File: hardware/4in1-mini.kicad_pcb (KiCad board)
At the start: 6 copper layers, 31.2 x 33 mm, 191 parts, among them J1 SM08B-SRSS-TB, Q1 DOY180N03T, Q10 DOY180N03T, Q11 DOY180N03T, Q12 DOY180N03T, Q13 DOY180N03T, Q14 DOY180N03T, Q15 DOY180N03T, Q16 DOY180N03T, Q17 DOY180N03T, Q18 DOY180N03T, Q19 DOY180N03T, Q2 DOY180N03T, Q20 DOY180N03T, Q21 DOY180N03T, Q22 DOY180N03T, Q23 DOY180N03T, Q24 DOY180N03T, Q3 DOY180N03T, Q4 DOY180N03T, Q5 DOY180N03T, Q6 DOY180N03T, Q7 DOY180N03T, Q8 DOY180N03T, Q9 DOY180N03T, U1 TLV76733DRVR, U10 AT32F421G8U7, U11 NSG2065Q, U12 INA186A3IDCKR, U13 LMR54406DBVR, U2 AT32F421G8U7, U3 NSG2065Q, U5 FTC160808S4R7MBCA, U6 AT32F421G8U7, U7 NSG2065Q, U8 AT32F421G8U7, U9 NSG2065Q

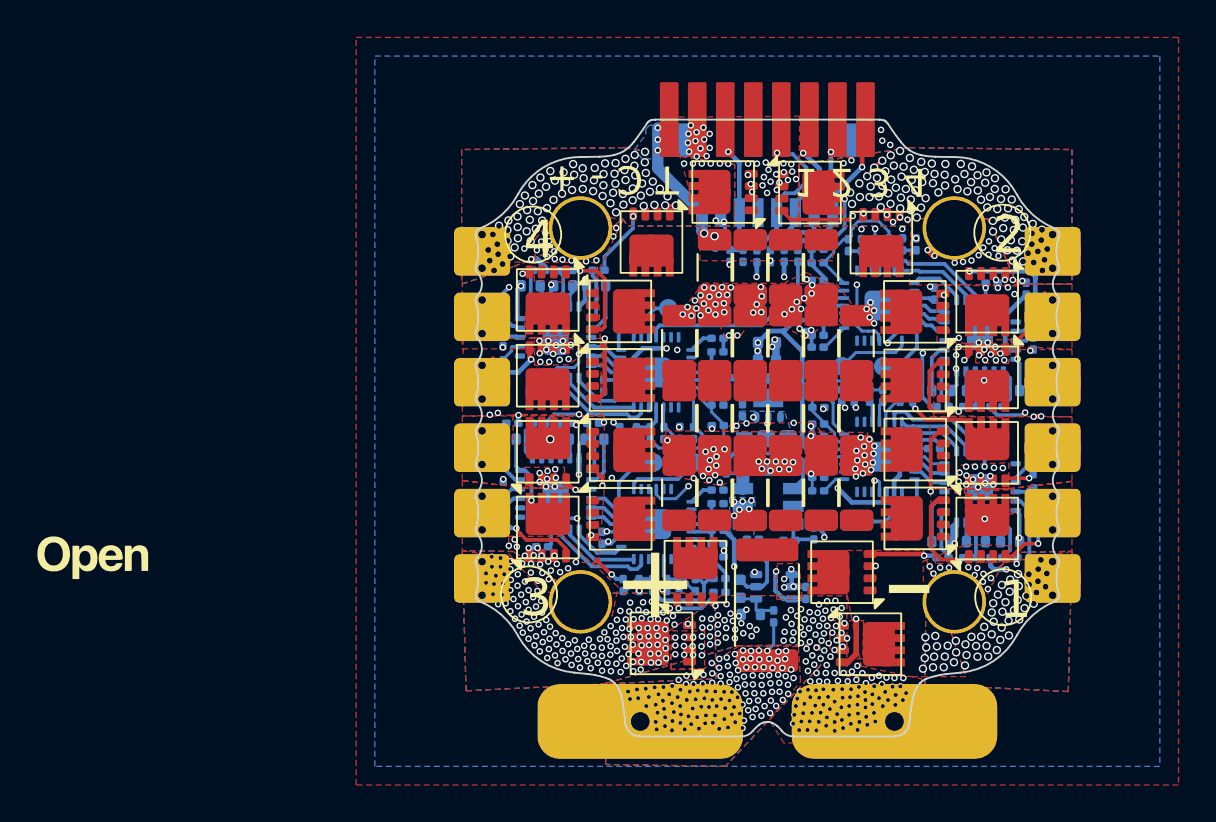
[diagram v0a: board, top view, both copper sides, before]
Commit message: Rebrand silkscreen to incutec, add via stitching, 4.7uF bulk caps
Board state for the batch-1 quote round: OpenDrone silkscreen replaced
with incutec (Stan), added via cluster near the FET bank (Stan), bulk
cap bank fields swapped to FH 1206B475K500NT 4.7uF 50V C29823 (from
the committed schematic change). Fabrication Toolkit archive name
moved to the org standard OpenESC-20x20-rev3.2.

Co-Authored-By: Claude Fable 5 <noreply@anthropic.com>
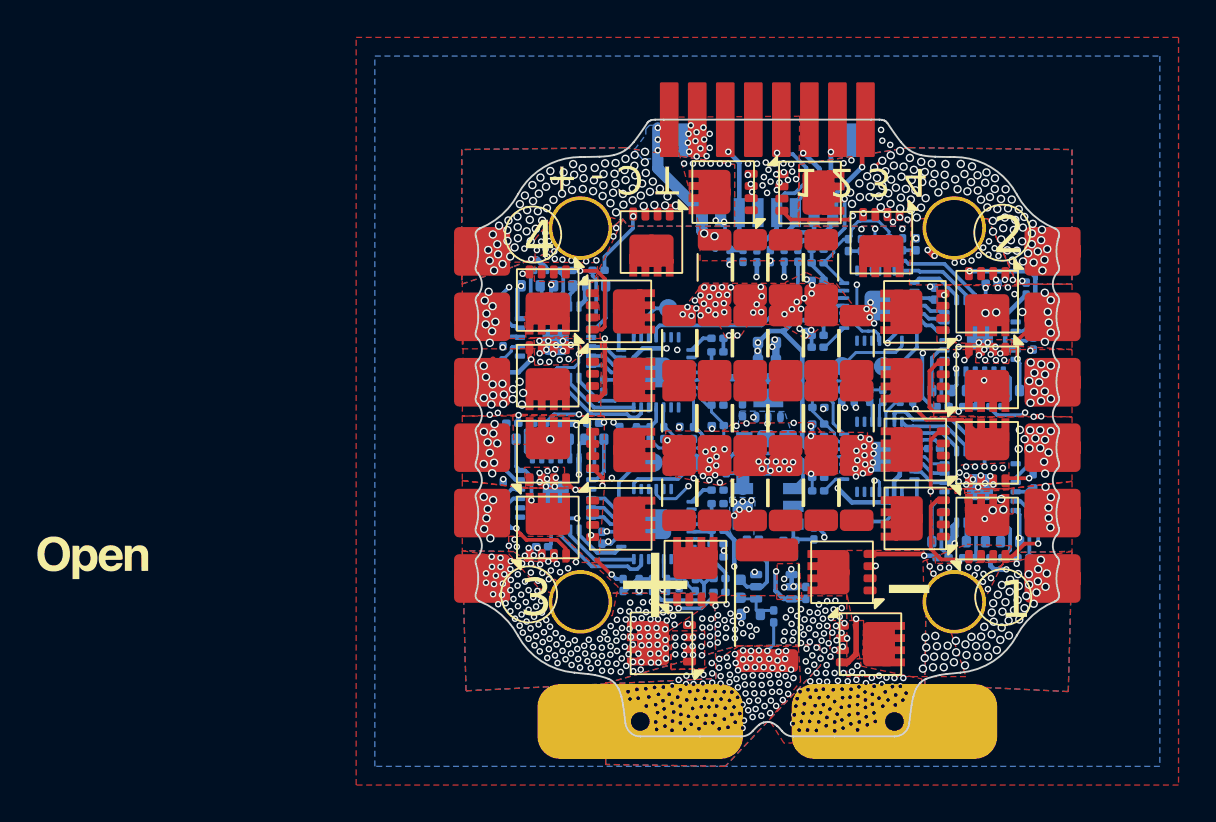
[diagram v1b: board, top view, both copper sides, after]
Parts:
- CL32, CL33, CL34, CL35, CL36, CL38, CL39, CL40, CL42, CL43, CL44, CL45, CL46, CL47, CL48, CL49, CL50 (x2), CL51 (x2), CL54, CL55: value 10uF -> 4.7uF
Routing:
- net /ESC4/MotorC: vias 2 -> 16
- net /ESC4/MotorB: vias 2 -> 10
- net /ESC3/MotorC: vias 2 -> 8
- net /ESC3/MotorB: vias 2 -> 11
- net /ESC2/MotorC: vias 2 -> 11
- net /ESC2/MotorB: vias 2 -> 14
- net /ESC1/MotorC: vias 2 -> 15
- net /ESC1/MotorB: vias 2 -> 10

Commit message: Sync silkscreen rev text to rev3.2 (pipeline rev sync)
Co-Authored-By: Claude Fable 5 <noreply@anthropic.com>
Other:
- board text added: "rev3.2"
- board text removed: "rev3.1"
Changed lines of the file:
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@@
 	)
 	(paper "A4")
+	(title_block
+		(rev "rev3.2")
+	)
 	(layers
 		(0 "F.Cu" signal)
@@
 		)
 	)
-	(gr_text "rev3.1"
+	(gr_text "rev3.2"
 		(at 80.4 38.75 0)
 		(layer "B.SilkS")
@@
 			(justify right bottom mirror)
 		)
-		(render_cache "rev3.1" 0
+		(render_cache "rev3.2" 0
 			(polygon
 				(pts
-					(xy 84.031402 38.495) (xy 83.785663 38.495) (xy 83.785663 37.879508) (xy 83.755804 37.879508) (xy 83.615945 38.495)
-					(xy 83.363794 38.495) (xy 83.51089 37.845619) (xy 83.479382 37.818416) (xy 83.444111 37.774597)
-					(xy 83.423406 37.726226) (xy 83.416368 37.671596) (xy 83.416368 37.30285) (xy 83.662107 37.30285)
-					(xy 83.662107 37.598231) (xy 83.672731 37.623236) (xy 83.696178 37.633586) (xy 83.785663 37.633586)
-					(xy 83.785663 37.269603) (xy 83.696178 37.269603) (xy 83.672731 37.279036) (xy 83.662107 37.30285)
-					(xy 83.416368 37.30285) (xy 83.416368 37.233333) (xy 83.423379 37.177251) (xy 83.443864 37.128238)
-					(xy 83.478466 37.084497) (xy 83.522874 37.05053) (xy 83.571817 37.030499) (xy 83.626936 37.023681)
-					(xy 84.031402 37.023681)
+					(xy 84.39337 38.495) (xy 84.147631 38.495) (xy 84.147631 37.879508) (xy 84.117772 37.879508) (xy 83.977913 38.495)
+					(xy 83.725762 38.495) (xy 83.872858 37.845619) (xy 83.84135 37.818416) (xy 83.806079 37.774597)
+					(xy 83.785374 37.726226) (xy 83.778336 37.671596) (xy 83.778336 37.30285) (xy 84.024075 37.30285)
+					(xy 84.024075 37.598231) (xy 84.034699 37.623236) (xy 84.058146 37.633586) (xy 84.147631 37.633586)
+					(xy 84.147631 37.269603) (xy 84.058146 37.269603) (xy 84.034699 37.279036) (xy 84.024075 37.30285)
+					(xy 83.778336 37.30285) (xy 83.778336 37.233333) (xy 83.785347 37.177251) (xy 83.805832 37.128238)
+					(xy 83.840434 37.084497) (xy 83.884842 37.05053) (xy 83.933785 37.030499) (xy 83.988904 37.023681)
+					(xy 84.39337 37.023681)
 				)
 			)
 			(polygon
 				(pts
-					(xy 82.650941 37.269603) (xy 83.017763 37.269603) (xy 83.017763 37.633586) (xy 82.77404 37.633586)
-					(xy 82.77404 37.879508) (xy 83.017763 37.879508) (xy 83.017763 38.249077) (xy 82.650941 38.249077)
-					(xy 82.650941 38.495) (xy 83.263502 38.495) (xy 83.263502 37.023681) (xy 82.650941 37.023681)
+					(xy 83.012909 37.269603) (xy 83.379731 37.269603) (xy 83.379731 37.633586) (xy 83.136008 37.633586)
+					(xy 83.136008 37.879508) (xy 83.379731 37.879508) (xy 83.379731 38.249077) (xy 83.012909 38.249077)
+					(xy 83.012909 38.495) (xy 83.62547 38.495) (xy 83.62547 37.023681) (xy 83.012909 37.023681)
 				)
 			)
 			(polygon
 				(pts
-					(xy 82.180529 37.023681) (xy 81.934791 37.023681) (xy 81.934791 38.11453) (xy 81.941905 38.191204)
-					(xy 81.962704 38.260666) (xy 81.997189 38.324446) (xy 82.04644 38.383625) (xy 82.105689 38.432735)
-					(xy 82.169568 38.46714) (xy 82.23916 38.487898) (xy 82.315993 38.495) (xy 82.549825 38.495) (xy 82.549825 37.023681)
-					(xy 82.304086 37.023681) (xy 82.304086 38.249077) (xy 82.256681 38.240135) (xy 82.216799 38.213357)
-					(xy 82.189577 38.173902) (xy 82.180529 38.12717)
+					(xy 82.542497 37.023681) (xy 82.296759 37.023681) (xy 82.296759 38.11453) (xy 82.303873 38.191204)
+					(xy 82.324672 38.260666) (xy 82.359157 38.324446) (xy 82.408408 38.383625) (xy 82.467657 38.432735)
+					(xy 82.531536 38.46714) (xy 82.601128 38.487898) (xy 82.677961 38.495) (xy 82.911793 38.495) (xy 82.911793 37.023681)
+					(xy 82.666054 37.023681) (xy 82.666054 38.249077) (xy 82.618649 38.240135) (xy 82.578767 38.213357)
+					(xy 82.551545 38.173902) (xy 82.542497 38.12717)
 				)
 			)
 			(polygon
 				(pts
-					(xy 81.60204 38.495) (xy 81.658501 38.488078) (xy 81.70776 38.467893) (xy 81.751608 38.433908)
-					(xy 81.785588 38.390058) (xy 81.805775 38.34077) (xy 81.8127 38.284248) (xy 81.8127 38.004071)
-					(xy 81.566961 38.004071) (xy 81.566961 38.249077) (xy 81.443405 38.249077) (xy 81.443405 37.978792)
-					(xy 81.450503 37.941421) (xy 81.471981 37.909091) (xy 81.503849 37.886954) (xy 81.542781 37.879508)
-					(xy 81.690884 37.879508) (xy 81.690884 37.633586) (xy 81.542781 37.633586) (xy 81.503805 37.62626)
-					(xy 81.471981 37.604551) (xy 81.450492 37.572679) (xy 81.443405 37.535858) (xy 81.443405 37.269603)
-					(xy 81.566961 37.269603) (xy 81.566961 37.510853) (xy 81.8127 37.510853) (xy 81.8127 37.232783)
-					(xy 81.805785 37.176761) (xy 81.785611 37.127867) (xy 81.751608 37.084314) (xy 81.707793 37.050603)
-					(xy 81.658532 37.030559) (xy 81.60204 37.023681) (xy 81.408325 37.023681) (xy 81.353201 37.03049)
-					(xy 81.304258 37.050494) (xy 81.259856 37.084405) (xy 81.225197 37.128095) (xy 81.204685 37.177046)
-					(xy 81.197666 37.233058) (xy 81.197666 37.547215) (xy 81.204764 37.603171) (xy 81.225526 37.652119)
-					(xy 81.26068 37.695867) (xy 81.321588 37.756592) (xy 81.26068 37.817775) (xy 81.22555 37.861821)
-					(xy 81.204774 37.911162) (xy 81.197666 37.967618) (xy 81.197666 38.283974) (xy 81.204696 38.340485)
-					(xy 81.22522 38.38983) (xy 81.259856 38.433817) (xy 81.30429 38.468003) (xy 81.353231 38.488146)
-					(xy 81.408325 38.495)
+					(xy 81.964008 38.495) (xy 82.020469 38.488078) (xy 82.069728 38.467893) (xy 82.113576 38.433908)
+					(xy 82.147556 38.390058) (xy 82.167743 38.34077) (xy 82.174668 38.284248) (xy 82.174668 38.004071)
+					(xy 81.928929 38.004071) (xy 81.928929 38.249077) (xy 81.805373 38.249077) (xy 81.805373 37.978792)
+					(xy 81.812471 37.941421) (xy 81.833949 37.909091) (xy 81.865817 37.886954) (xy 81.904749 37.879508)
+					(xy 82.052852 37.879508) (xy 82.052852 37.633586) (xy 81.904749 37.633586) (xy 81.865773 37.62626)
+					(xy 81.833949 37.604551) (xy 81.81246 37.572679) (xy 81.805373 37.535858) (xy 81.805373 37.269603)
+					(xy 81.928929 37.269603) (xy 81.928929 37.510853) (xy 82.174668 37.510853) (xy 82.174668 37.232783)
+					(xy 82.167753 37.176761) (xy 82.147579 37.127867) (xy 82.113576 37.084314) (xy 82.069761 37.050603)
+					(xy 82.0205 37.030559) (xy 81.964008 37.023681) (xy 81.770293 37.023681) (xy 81.715169 37.03049)
+					(xy 81.666226 37.050494) (xy 81.621824 37.084405) (xy 81.587165 37.128095) (xy 81.566653 37.177046)
+					(xy 81.559634 37.233058) (xy 81.559634 37.547215) (xy 81.566732 37.603171) (xy 81.587494 37.652119)
+					(xy 81.622648 37.695867) (xy 81.683556 37.756592) (xy 81.622648 37.817775) (xy 81.587518 37.861821)
+					(xy 81.566742 37.911162) (xy 81.559634 37.967618) (xy 81.559634 38.283974) (xy 81.566664 38.340485)
+					(xy 81.587188 38.38983) (xy 81.621824 38.433817) (xy 81.666258 38.468003) (xy 81.715199 38.488146)
+					(xy 81.770293 38.495)
 				)
 			)
 			(polygon
 				(pts
-					(xy 80.837163 38.495) (xy 81.082902 38.495) (xy 81.082902 38.249077) (xy 80.837163 38.249077)
+					(xy 81.199131 38.495) (xy 81.44487 38.495) (xy 81.44487 38.249077) (xy 81.199131 38.249077)
 				)
 			)
 			(polygon
 				(pts
-					(xy 80.470799 38.495) (xy 80.716538 38.495) (xy 80.716538 37.145588) (xy 80.594722 37.023681) (xy 80.470799 37.023681)
+					(xy 81.084368 38.495) (xy 81.084368 37.842596) (xy 81.07749 37.787411) (xy 81.05733 37.738732)
+					(xy 81.023185 37.69486) (xy 80.979265 37.660767) (xy 80.929946 37.640526) (xy 80.873433 37.633586)
+					(xy 80.715072 37.633586) (xy 80.715072 37.269603) (xy 80.838629 37.269603) (xy 80.838629 37.510853)
+					(xy 81.084368 37.510853) (xy 81.084368 37.232783) (xy 81.077462 37.176755) (xy 81.057316 37.12786)
+					(xy 81.023368 37.084314) (xy 80.979552 37.050603) (xy 80.930292 37.030559) (xy 80.8738 37.023681)
+					(xy 80.679993 37.023681) (xy 80.624875 37.030499) (xy 80.575932 37.05053) (xy 80.531524 37.084497)
+					(xy 80.496871 37.128247) (xy 80.476356 37.177288) (xy 80.469334 37.233424) (xy 80.469334 37.671871)
+					(xy 80.476307 37.726607) (xy 80.496793 37.774979) (xy 80.531616 37.818691) (xy 80.576084 37.852651)
+					(xy 80.625117 37.872686) (xy 80.680359 37.879508) (xy 80.838629 37.879508) (xy 80.838629 38.249077)
+					(xy 80.715072 38.249077) (xy 80.715072 38.004071) (xy 80.469334 38.004071) (xy 80.469334 38.495)
 				)
 			)

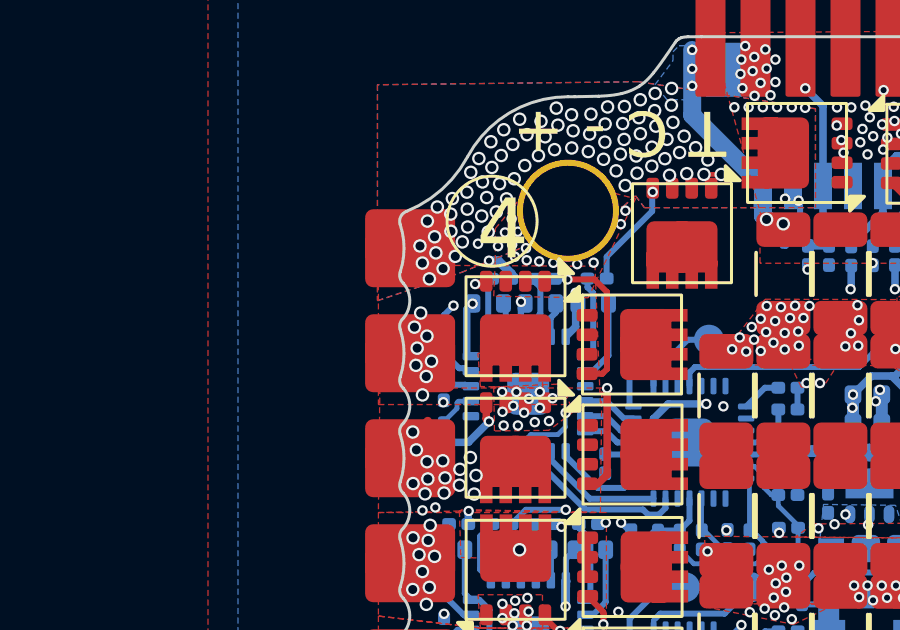
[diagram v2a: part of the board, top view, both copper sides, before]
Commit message: Sync silkscreen rev text to rev3.3 (pipeline rev sync)
Co-Authored-By: Claude Fable 5 <noreply@anthropic.com>
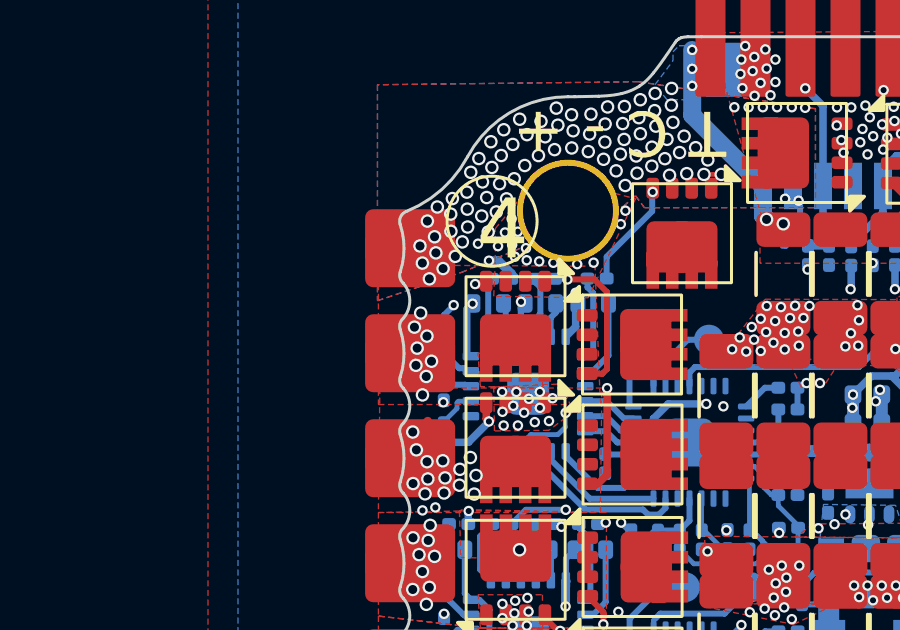
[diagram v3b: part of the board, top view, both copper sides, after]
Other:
- board text added: "rev3.3"
- board text removed: "rev3.2"
